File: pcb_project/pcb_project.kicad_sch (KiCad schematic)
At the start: 15 parts, among them J1 Conn_01x10_Pin

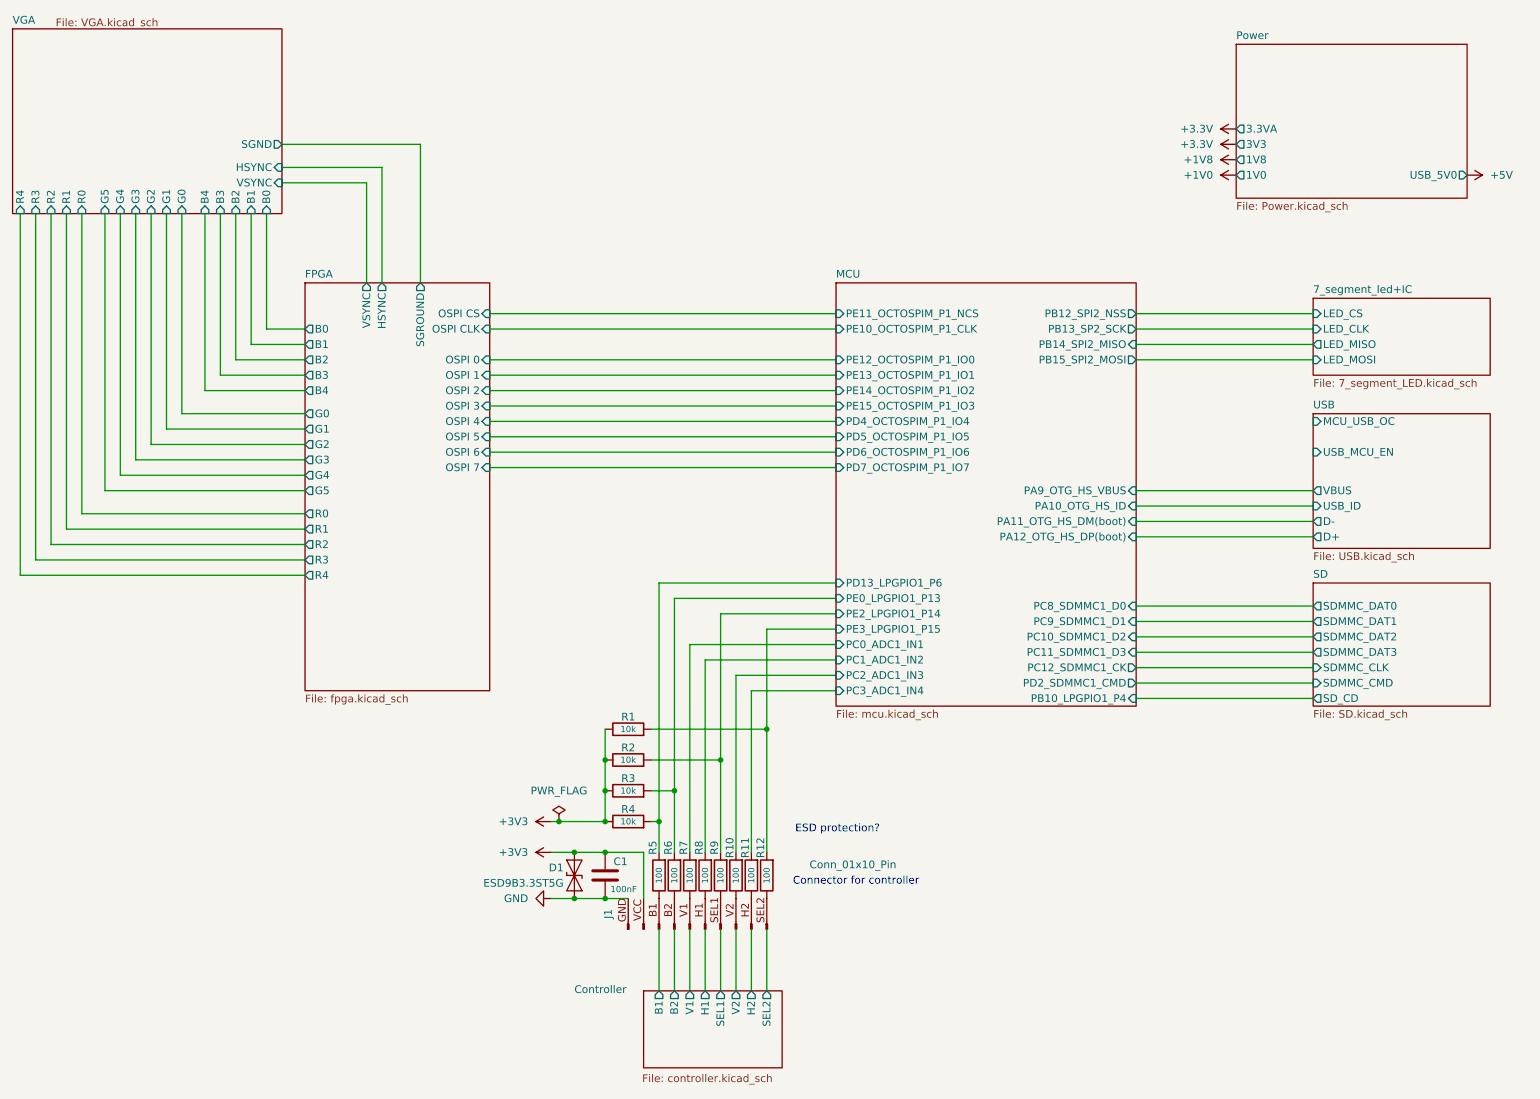
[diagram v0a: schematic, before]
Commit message: Fix USB pins and other ERC errors
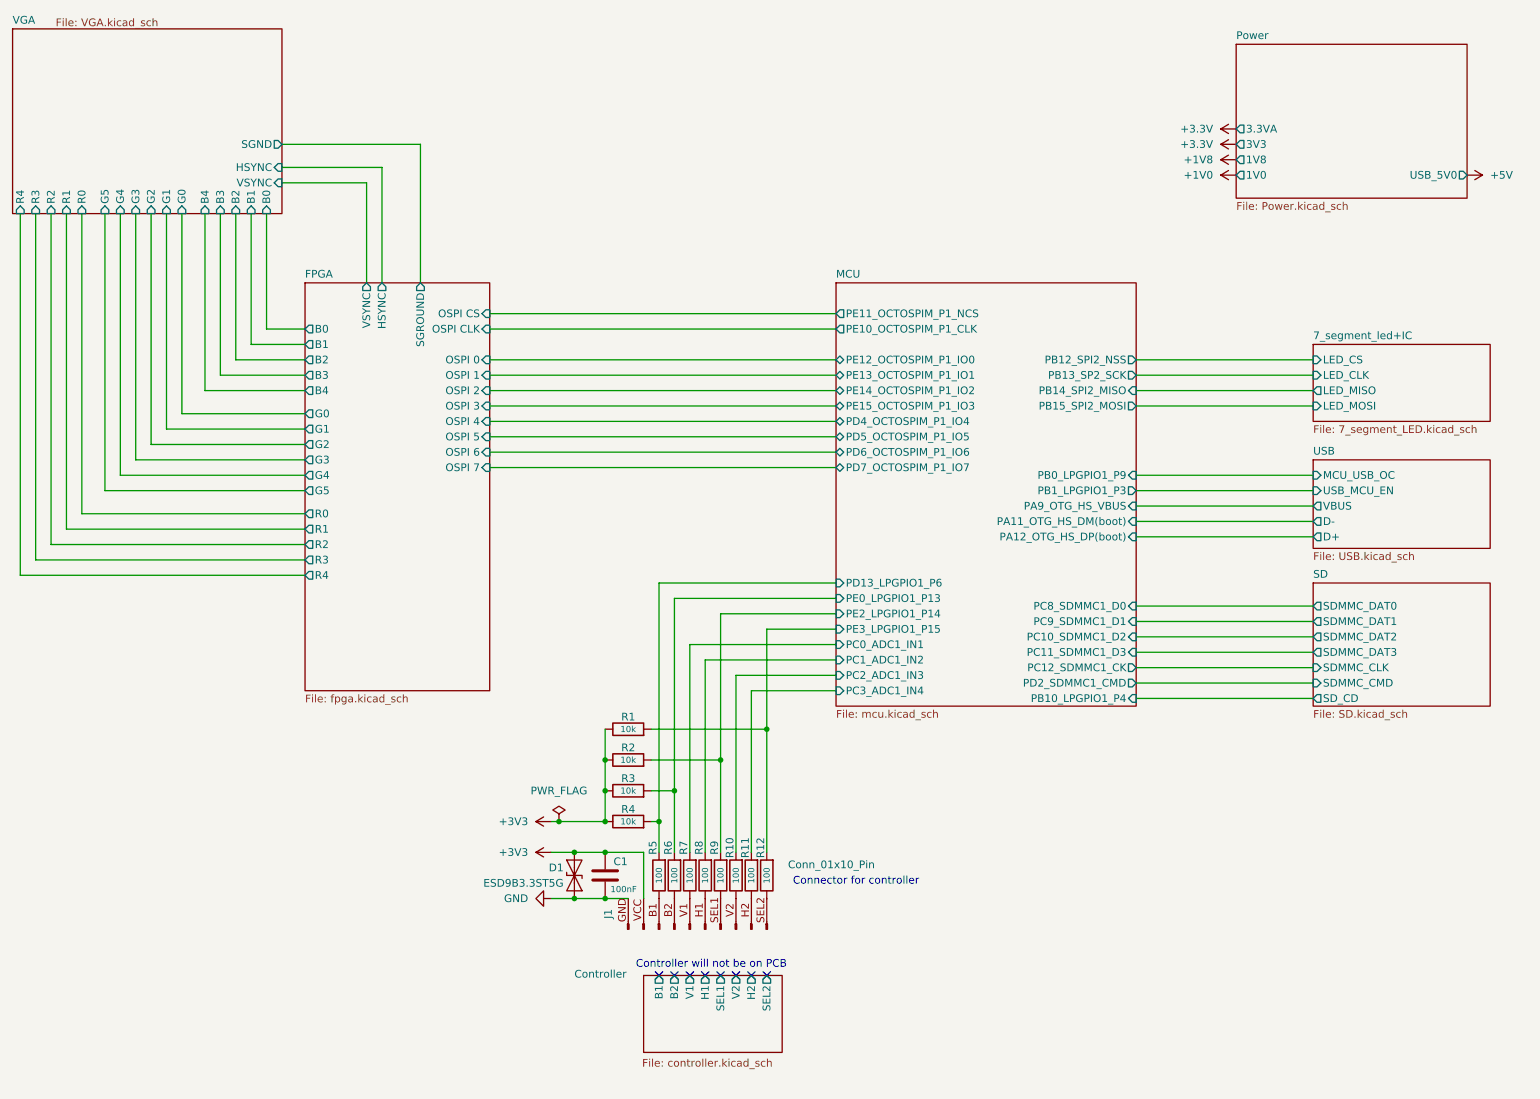
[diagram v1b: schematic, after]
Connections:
- no-connect marks 0 -> 8
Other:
- sheet MCU ports: added PB0_LPGPIO1_P9, PB1_LPGPIO1_P3; removed PA10_OTG_HS_ID
- sheet USB ports: added none; removed USB_ID
- note added: "Controller will not be on PCB"
- note removed: "ESD protection?"

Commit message: Fix JTAG connector, add pullups (FPGA has internal pullups as well), add some capacitor footprints
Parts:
- C1: footprint (none) -> Capacitor_SMD:C_0603_1608Metric_Pad1.08x0.95mm_HandSolder
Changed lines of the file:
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@@
 			)
 		)
-		(property "Footprint" ""
+		(property "Footprint" "Capacitor_SMD:C_0603_1608Metric_Pad1.08x0.95mm_HandSolder"
 			(at 124.1552 166.37 0)
 			(effects

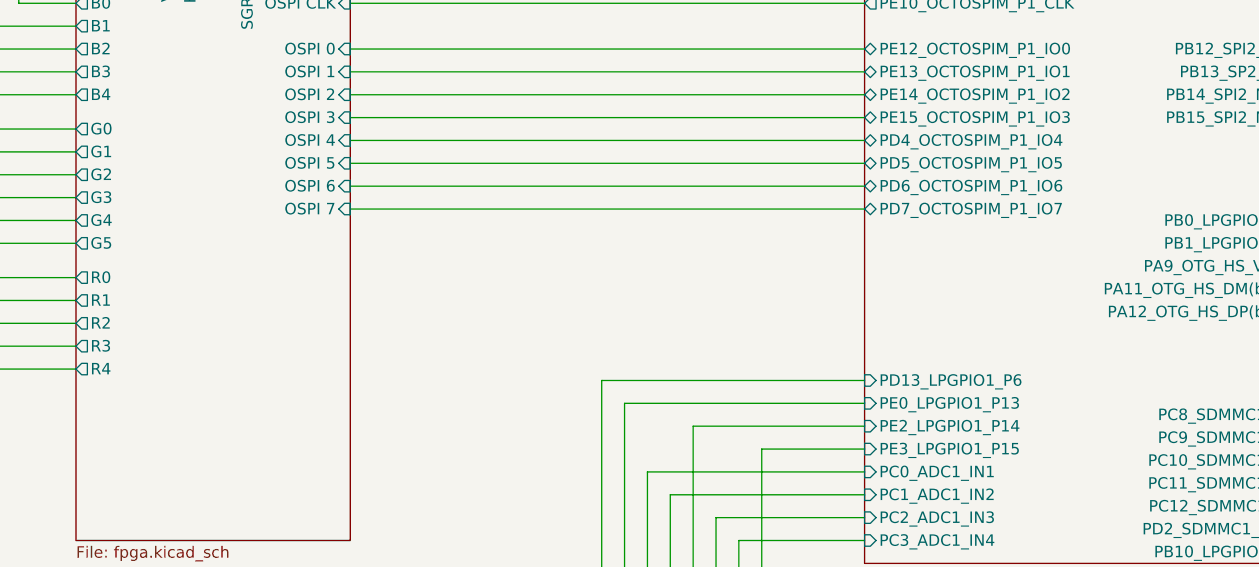
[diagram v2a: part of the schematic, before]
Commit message: Add FPGA DONE AND PROGRAM_B (reset) to MCU GPIO
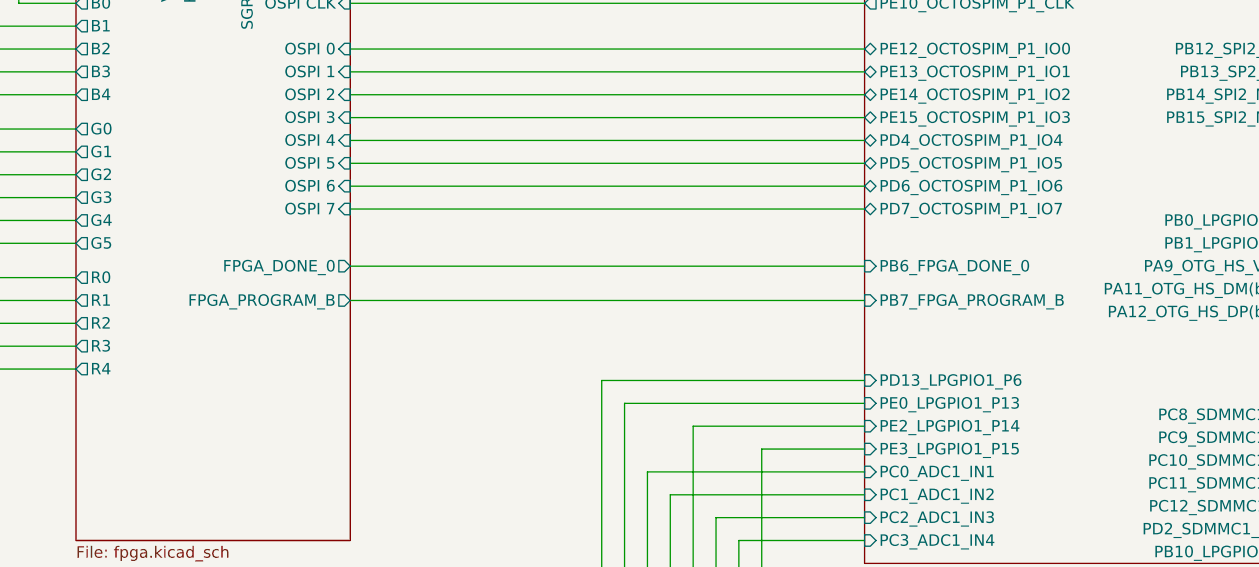
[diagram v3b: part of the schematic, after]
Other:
- sheet FPGA ports: added FPGA_DONE_0, FPGA_PROGRAM_B; removed none
- sheet MCU ports: added PB6_FPGA_DONE_0, PB7_FPGA_PROGRAM_B; removed none
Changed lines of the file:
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@@
+	(wire
+		(pts
+			(xy 104.14 101.6) (xy 161.29 101.6)
+		)
+		(stroke
+			(width 0)
+			(type default)
+		)
+	)
 	(wire
 		(pts
@@
 		(pts
 			(xy 31.75 107.95) (xy 31.75 53.34)
+		)
+		(stroke
+			(width 0)
+			(type default)
+		)
+	)
+	(wire
+		(pts
+			(xy 104.14 105.41) (xy 161.29 105.41)
 		)
 		(stroke
@@
 			)
 		)
+		(pin "PB6_FPGA_DONE_0" input
+			(at 161.29 101.6 180)
+			(effects
+				(font
+					(size 1.27 1.27)
+				)
+				(justify left)
+			)
+		)
+		(pin "PB7_FPGA_PROGRAM_B" input
+			(at 161.29 105.41 180)
+			(effects
+				(font
+					(size 1.27 1.27)
+				)
+				(justify left)
+			)
+		)
 		(instances
 			(project "pcb_project"
@@
 			)
 		)
+		(pin "FPGA_DONE_0" output
+			(at 104.14 101.6 0)
+			(effects
+				(font
+					(size 1.27 1.27)
+				)
+				(justify right)
+			)
+		)
+		(pin "FPGA_PROGRAM_B" output
+			(at 104.14 105.41 0)
+			(effects
+				(font
+					(size 1.27 1.27)
+				)
+				(justify right)
+			)
+		)

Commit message: Forgot CTRL +S lol
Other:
- added sheet I2C level shifting (I2ClevelShifiting.kicad_sch)
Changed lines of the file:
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@@
+	)
+	(sheet
+		(at 134.62 26.67)
+		(size 21.59 12.7)
+		(exclude_from_sim no)
+		(in_bom yes)
+		(on_board yes)
+		(dnp no)
+		(fields_autoplaced yes)
+		(stroke
+			(width 0.1524)
+			(type solid)
+		)
+		(fill
+			(color 0 0 0 0.0000)
+		)
+		(property "Sheetname" "I2C level shifting"
+			(at 134.62 25.9584 0)
+			(effects
+				(font
+					(size 1.27 1.27)
+				)
+				(justify left bottom)
+			)
+		)
+		(property "Sheetfile" "I2ClevelShifiting.kicad_sch"
+			(at 134.62 39.9546 0)
+			(effects
+				(font
+					(size 1.27 1.27)
+				)
+				(justify left top)
+			)
+		)
+		(instances
+			(project "pcb_project"
+				(path "/98f80f66-4595-4d0f-90ca-59b2db6f447b"
+					(page "12")
+				)
+			)
+		)
 	)
 	(sheet

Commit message: Add most footprints, missing some inductors and 3 buttons
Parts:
- J1: footprint (none) -> Connector_PinHeader_2.54mm:PinHeader_1x10_P2.54mm_Vertical
- R1, R10, R11, R12, R2, R3, R4, R5, R6, R7, R8, R9: footprint (none) -> Resistor_SMD:R_0805_2012Metric_Pad1.20x1.40mm_HandSolder
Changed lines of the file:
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@@
 			)
 		)
-		(property "Footprint" ""
+		(property "Footprint" "Resistor_SMD:R_0805_2012Metric_Pad1.20x1.40mm_HandSolder"
 			(at 133.858 162.56 90)
 			(effects
@@
 			)
 		)
-		(property "Footprint" ""
+		(property "Footprint" "Resistor_SMD:R_0805_2012Metric_Pad1.20x1.40mm_HandSolder"
 			(at 136.398 162.56 90)
 			(effects
@@
 			)
 		)
-		(property "Footprint" ""
+		(property "Footprint" "Resistor_SMD:R_0805_2012Metric_Pad1.20x1.40mm_HandSolder"
 			(at 127 140.208 90)
 			(effects
@@
 			)
 		)
-		(property "Footprint" ""
+		(property "Footprint" "Resistor_SMD:R_0805_2012Metric_Pad1.20x1.40mm_HandSolder"
 			(at 141.478 162.56 90)
 			(effects
@@
 			)
 		)
-		(property "Footprint" ""
+		(property "Footprint" "Resistor_SMD:R_0805_2012Metric_Pad1.20x1.40mm_HandSolder"
 			(at 127 145.288 90)
 			(effects
@@
 			)
 		)
-		(property "Footprint" ""
+		(property "Footprint" "Resistor_SMD:R_0805_2012Metric_Pad1.20x1.40mm_HandSolder"
 			(at 151.638 162.56 90)
 			(effects
@@
 			)
 		)
-		(property "Footprint" ""
+		(property "Footprint" "Connector_PinHeader_2.54mm:PinHeader_1x10_P2.54mm_Vertical"
 			(at 137.16 171.45 0)
 			(effects
@@
 			)
 		)
-		(property "Footprint" ""
+		(property "Footprint" "Resistor_SMD:R_0805_2012Metric_Pad1.20x1.40mm_HandSolder"
 			(at 146.558 162.56 90)
 			(effects
@@
 			)
 		)
-		(property "Footprint" ""
+		(property "Footprint" "Resistor_SMD:R_0805_2012Metric_Pad1.20x1.40mm_HandSolder"
 			(at 127 155.448 90)
 			(effects
@@
 			)
 		)
-		(property "Footprint" ""
+		(property "Footprint" "Resistor_SMD:R_0805_2012Metric_Pad1.20x1.40mm_HandSolder"
 			(at 144.018 162.56 90)
 			(effects
@@
 			)
 		)
-		(property "Footprint" ""
+		(property "Footprint" "Resistor_SMD:R_0805_2012Metric_Pad1.20x1.40mm_HandSolder"
 			(at 127 150.368 90)
 			(effects
@@
 			)
 		)
-		(property "Footprint" ""
+		(property "Footprint" "Resistor_SMD:R_0805_2012Metric_Pad1.20x1.40mm_HandSolder"
 			(at 149.098 162.56 90)
 			(effects
@@
 			)
 		)
-		(property "Footprint" ""
+		(property "Footprint" "Resistor_SMD:R_0805_2012Metric_Pad1.20x1.40mm_HandSolder"
 			(at 138.938 162.56 90)
 			(effects

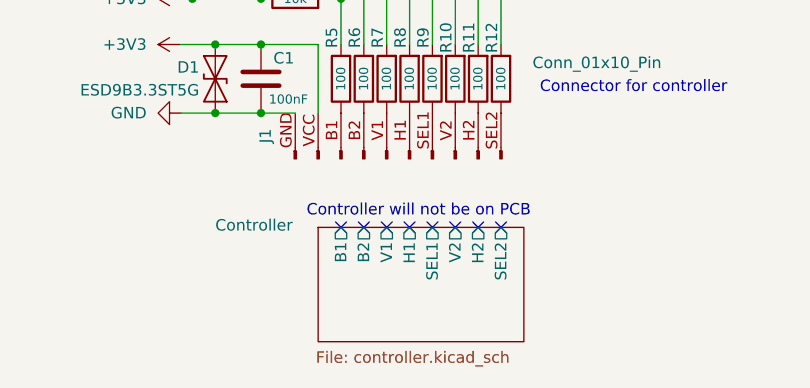
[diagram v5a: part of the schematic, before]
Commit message: Move controller to its own project
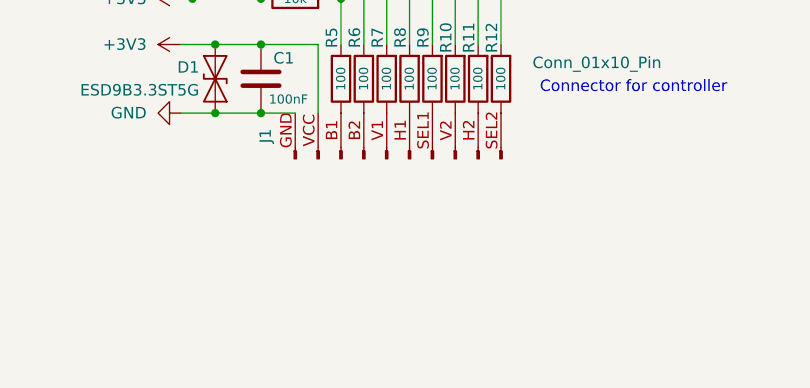
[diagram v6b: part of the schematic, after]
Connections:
- no-connect marks 8 -> 0
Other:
- removed sheet Controller
- note removed: "Controller will not be on PCB"
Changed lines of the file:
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@@
 	(generator_version "9.0")
 	(paper "A4")
-	(text "Controller will not be on PCB"
-		(exclude_from_sim no)
-		(at 140.716 177.292 0)
-		(effects
-			(font
-				(size 1.27 1.27)
-			)
-		)
-	)
 	(text "Connector for controller"
 		(exclude_from_sim no)
@@
 		(color 0 0 0 0)
 	)
-	(no_connect
-		(at 149.86 179.07)
-	)
-	(no_connect
-		(at 139.7 179.07)
-	)
-	(no_connect
-		(at 144.78 179.07)
-	)
-	(no_connect
-		(at 132.08 179.07)
-	)
-	(no_connect
-		(at 137.16 179.07)
-	)
-	(no_connect
-		(at 142.24 179.07)
-	)
-	(no_connect
-		(at 134.62 179.07)
-	)
-	(no_connect
-		(at 147.32 179.07)
-	)
 	(wire
 		(pts
@@
 				)
 			)
-		)
-	)
-	(sheet
-		(at 129.54 179.07)
-		(size 22.86 12.7)
-		(exclude_from_sim no)
-		(in_bom yes)
-		(on_board yes)
-		(dnp no)
-		(stroke
-			(width 0.1524)
-			(type solid)
-		)
-		(fill
-			(color 0 0 0 0.0000)
-		)
-		(property "Sheetname" "Controller"
-			(at 118.11 179.578 0)
-			(effects
-				(font
-					(size 1.27 1.27)
-				)
-				(justify left bottom)
-			)
-		)
-		(property "Sheetfile" "controller.kicad_sch"
-			(at 129.286 192.786 0)
-			(effects
-				(font
-					(size 1.27 1.27)
-				)
-				(justify left top)
-			)
-		)
-		(pin "B1" output
-			(at 132.08 179.07 90)
-			(effects
-				(font
-					(size 1.27 1.27)
-				)
-				(justify right)
-			)
-		)
-		(pin "V1" output
-			(at 137.16 179.07 90)
-			(effects
-				(font
-					(size 1.27 1.27)
-				)
-				(justify right)
-			)
-		)
-		(pin "SEL2" output
-			(at 149.86 179.07 90)
-			(effects
-				(font
-					(size 1.27 1.27)
-				)
-				(justify right)
-			)
-		)
-		(pin "SEL1" output
-			(at 142.24 179.07 90)
-			(effects
-				(font
-					(size 1.27 1.27)
-				)
-				(justify right)
-			)
-		)
-		(pin "H1" output
-			(at 139.7 179.07 90)
-			(effects
-				(font
-					(size 1.27 1.27)
-				)
-				(justify right)
-			)
-		)
-		(pin "H2" output
-			(at 147.32 179.07 90)
-			(effects
-				(font
-					(size 1.27 1.27)
-				)
-				(justify right)
-			)
-		)
-		(pin "B2" output
-			(at 134.62 179.07 90)
-			(effects
-				(font
-					(size 1.27 1.27)
-				)
-				(justify right)
-			)
-		)
-		(pin "V2" output
-			(at 144.78 179.07 90)
-			(effects
-				(font
-					(size 1.27 1.27)
-				)
-				(justify right)
-			)
-		)
-		(instances
-			(project "pcb_project"
-				(path "/98f80f66-4595-4d0f-90ca-59b2db6f447b"
-					(page "8")
-				)
-			)
